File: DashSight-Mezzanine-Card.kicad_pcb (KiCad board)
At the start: 4 copper layers, 72 x 78.5 mm, 72 parts, among them IC2 ELM327, J1 Pi2 Connector, J2 Euler Connector, J3 Conn_Coaxial, J4 OBD2-DB9_Male, J5 Conn_02x05_Odd_Even, Q1 2N3904, Q2 2N3906, Q3 2N3906, Q4 2N3904, Q5 2N3904, Q6 2N3904, Q7 2N3904, SW1 SW_Push, SW2 SW_Push, U1 MCP2561-E/P, U2 LM317L_TO92, U4 ADuM1201AR, U5 NEO-M9N, Y1 4.0MHz

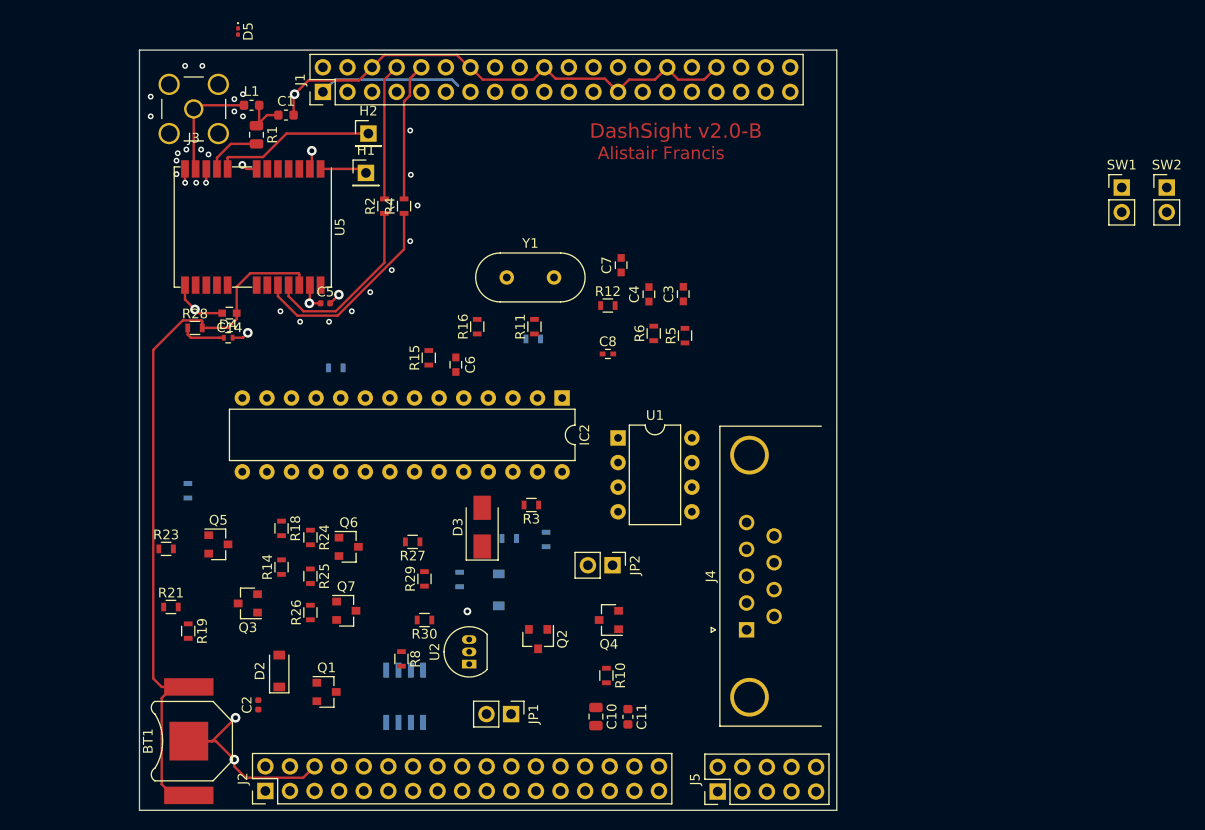
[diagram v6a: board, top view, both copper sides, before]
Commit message: pcb: Place and route the ELM327
Signed-off-by: Alistair Francis <alistair@alistair23.me>
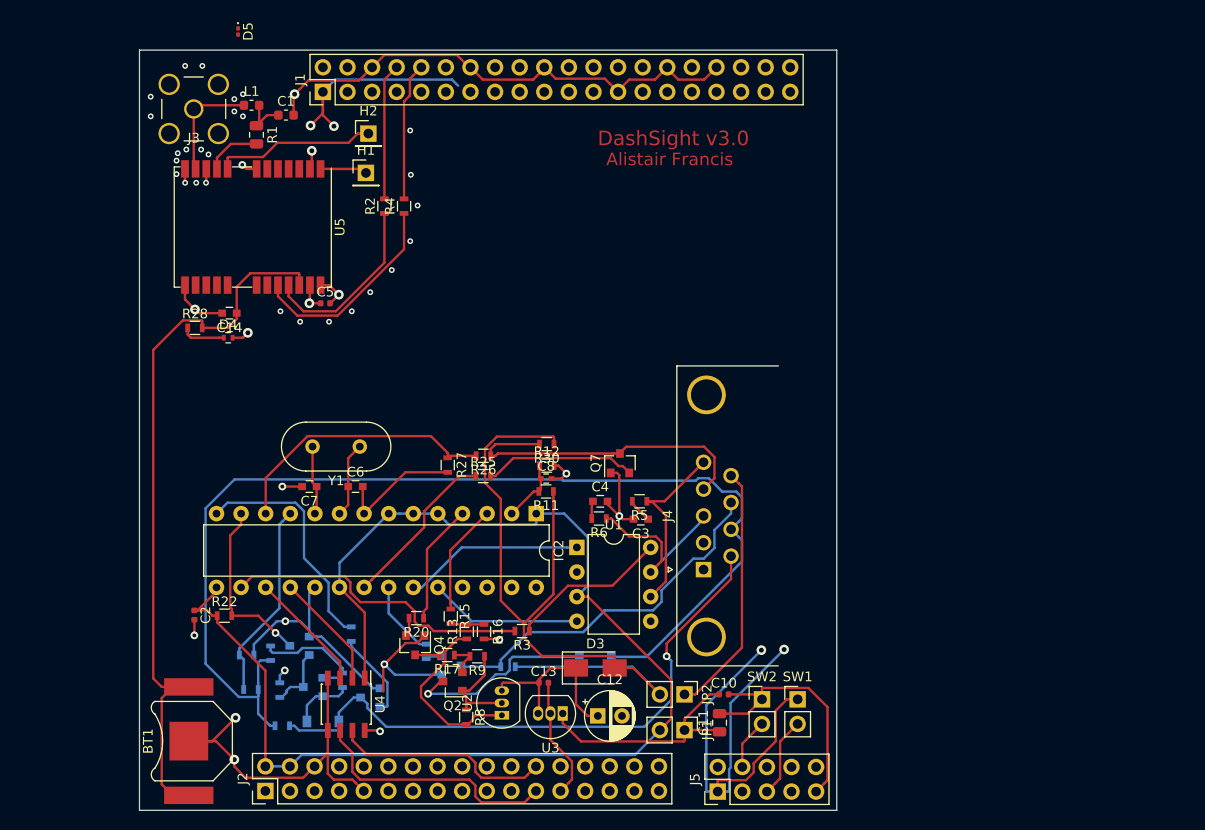
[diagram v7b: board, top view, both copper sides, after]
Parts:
- added C10: 0.1uF, Capacitor_SMD:C_0402_1005Metric, F.Cu at (188.3, 113.0)
- added C12: 2.2uF 50V, Capacitor_THT:CP_Radial_D5.0mm_P2.50mm, F.Cu at (175.3, 115.3)
- added U3: LP2950-3.0_TO92, Package_TO_SOT_THT:TO-92_Inline, F.Cu at (171.7, 115.0)
- C11: renamed from C10; value 10uF 10V -> 4.7uF 10V
- C13: renamed from C11; value 10uF -> 0.1uF 50V; footprint Capacitor_SMD:C_0603_1608Metric -> Capacitor_SMD:C_0402_1005Metric
- D2, Q1, Q3, Q5, Q6, R10, R14, R18, R19, R21, R23, R24, R29: moved to B.Cu
- R13, R17, R20, R22, R9, U4: moved to F.Cu
- moved SW2 67.4 mm to (192.3, 113.5)
- moved SW1 62.6 mm to (196.0, 113.5)
- moved C7 39.5 mm to (145.5, 91.6), turned to 180 degrees
- moved R10 33.9 mm to (142.7, 116.3), turned to 0 degrees
- moved Q7 32.1 mm to (177.6, 89.2), turned to 90 degrees
- moved R16 31.5 mm to (163.6, 106.6), turned to 270 degrees
- moved R20 31.3 mm to (156.6, 105.2), turned to 180 degrees
- moved R22 28.1 mm to (136.8, 104.9), turned to 0 degrees
- moved R15 26.8 mm to (160.1, 105.0), turned to 270 degrees
- moved R26 24.1 mm to (163.5, 88.4), turned to 180 degrees
- moved C3 23.7 mm to (179.8, 94.9), turned to 180 degrees
- moved Y1 23.1 mm to (150.7, 87.4), turned to 180 degrees
- moved R7 22.4 mm to (149.9, 106.8)
- moved R30 22.1 mm to (170.1, 87.2)
- moved C4 22.0 mm to (175.6, 93.1), turned to 0 degrees
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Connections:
- J5 pad 4: (no net) -> ResetSW
- SW2 pad 2: PowerOn -> ResetSW
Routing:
- net +5V: track 0.00 -> 135.1 mm
- net GND: track 85.6 -> 213.9 mm, vias 33 -> 41
- net J1850_Bus+: track 0.00 -> 115.3 mm
- net Vbat: track 0.00 -> 77.8 mm
- net J1850_Bus-: track 0.00 -> 62.5 mm, vias 0 -> 1
- net +3V3: track 21.9 -> 83.0 mm, vias 3 -> 8
- net ISO9141-2_L: track 0.00 -> 37.9 mm
- net ISO9141-2_K: track 0.00 -> 33.7 mm
- net PwrCntrl: track 0.00 -> 32.4 mm
- net ELM_Pin12: track 0.00 -> 28.5 mm
- net UART3_RX: track 0.00 -> 26.2 mm
- net Vbat-OBD: track 0.00 -> 26.2 mm
- net Net-(C10-Pad1): track 0.00 -> 25.3 mm
- net ELM_Pin14: track 0.00 -> 24.2 mm
- net UART3_TX: track 0.00 -> 22.6 mm
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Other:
- board text added: "DashSight v3.0"
- board text removed: "DashSight v2.0-B"

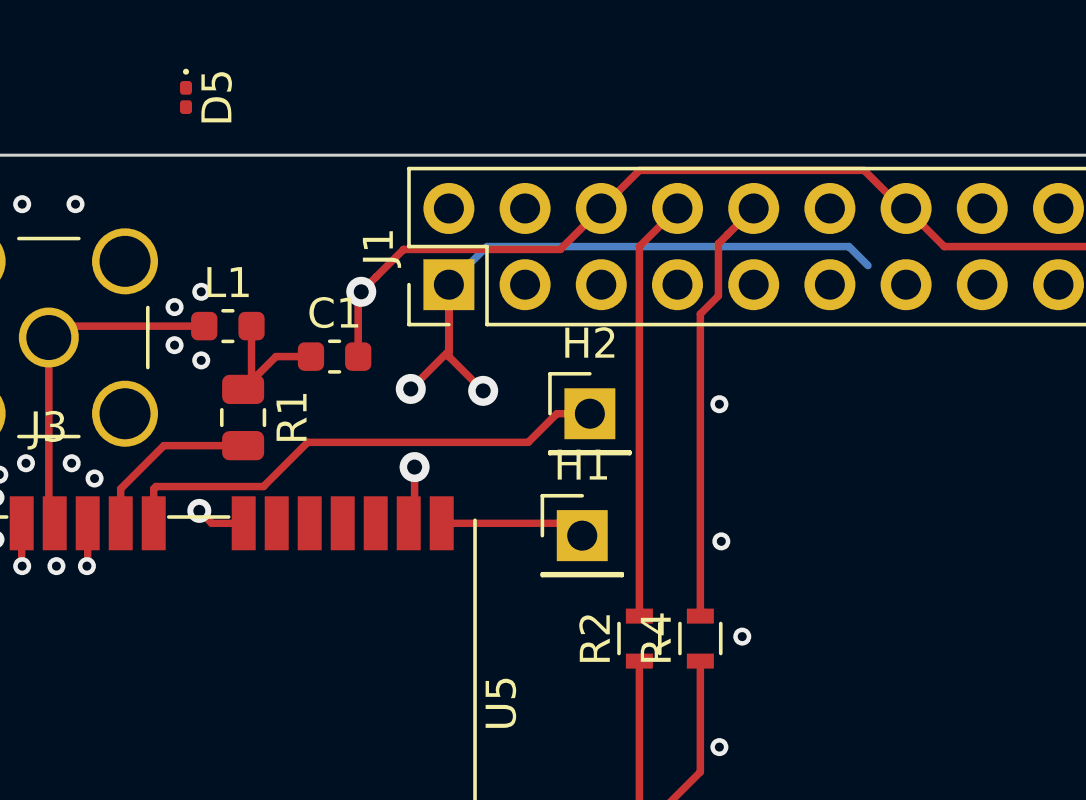
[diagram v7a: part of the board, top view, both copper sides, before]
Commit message: pcb: Connect the GNSS PPS
Signed-off-by: Alistair Francis <alistair@alistair23.me>
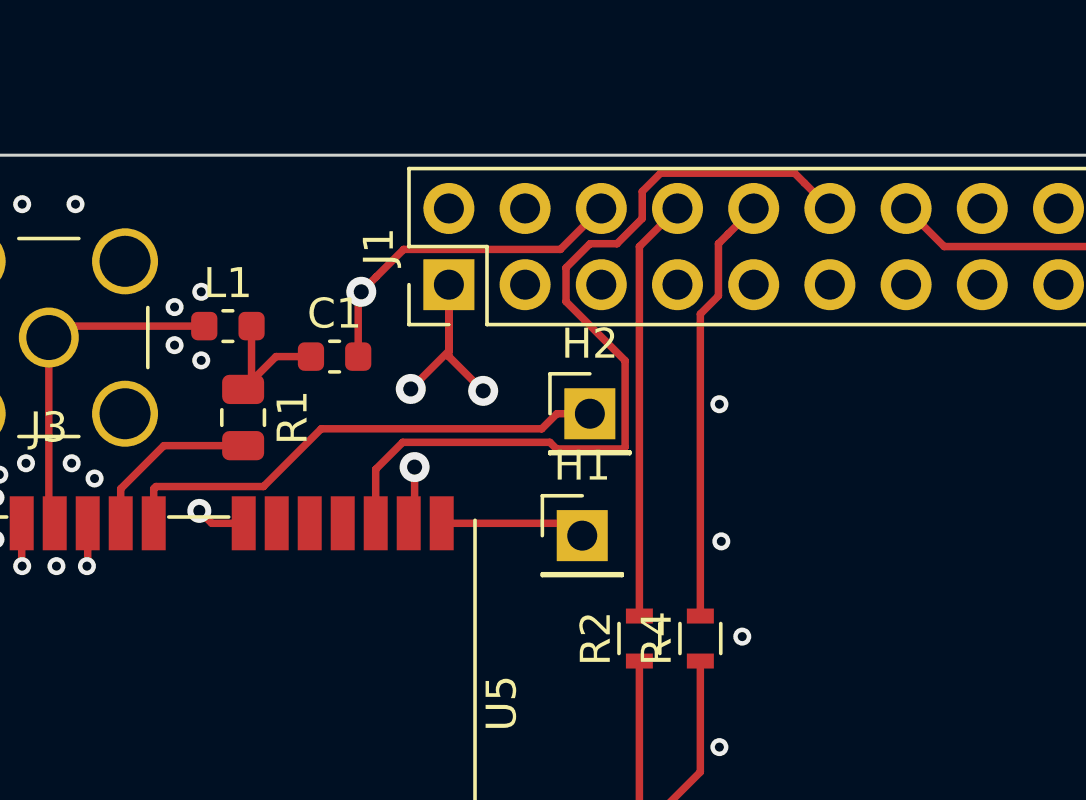
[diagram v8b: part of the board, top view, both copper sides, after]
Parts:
- removed D5: D_Zener, Diode_SMD:D_0201_0603Metric
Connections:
- J1 pad 12: (no net) -> PC8
- U5 pad 3: (no net) -> PC8
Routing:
- net PC8: track 0.00 -> 28.5 mm
- net +3V3: track 83.0 -> 68.3 mm
- net GND: track 213.9 -> 202.8 mm
